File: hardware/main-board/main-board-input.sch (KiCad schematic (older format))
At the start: 11 parts

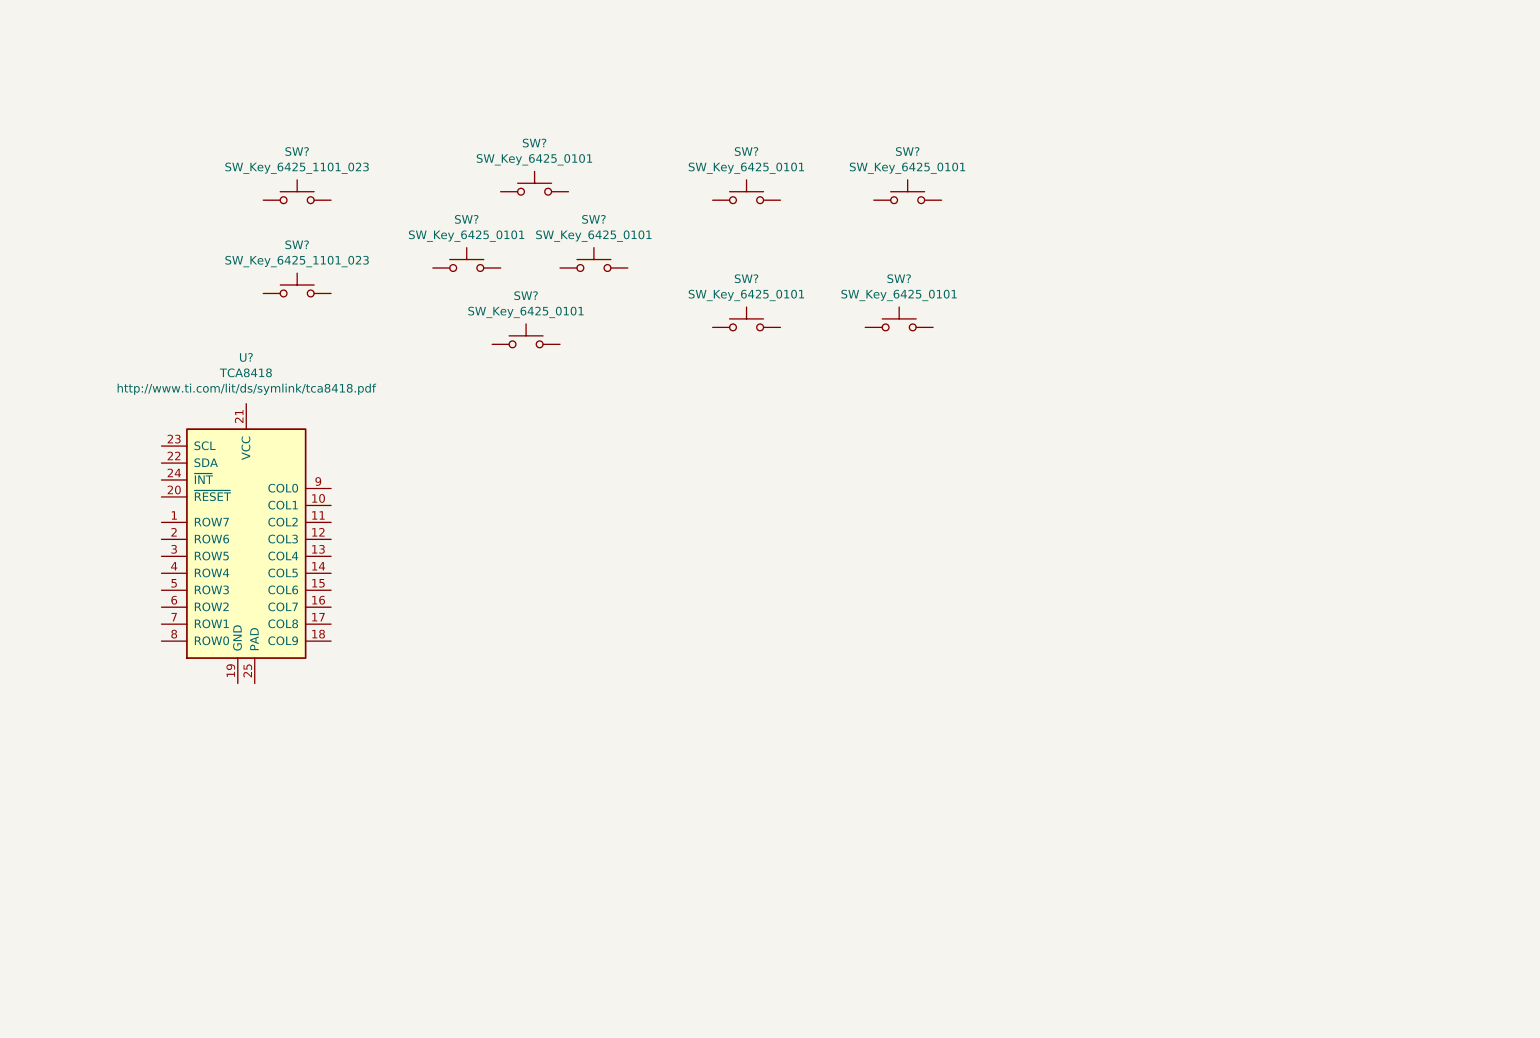
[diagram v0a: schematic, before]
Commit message: Starting to put main board MCU components in place
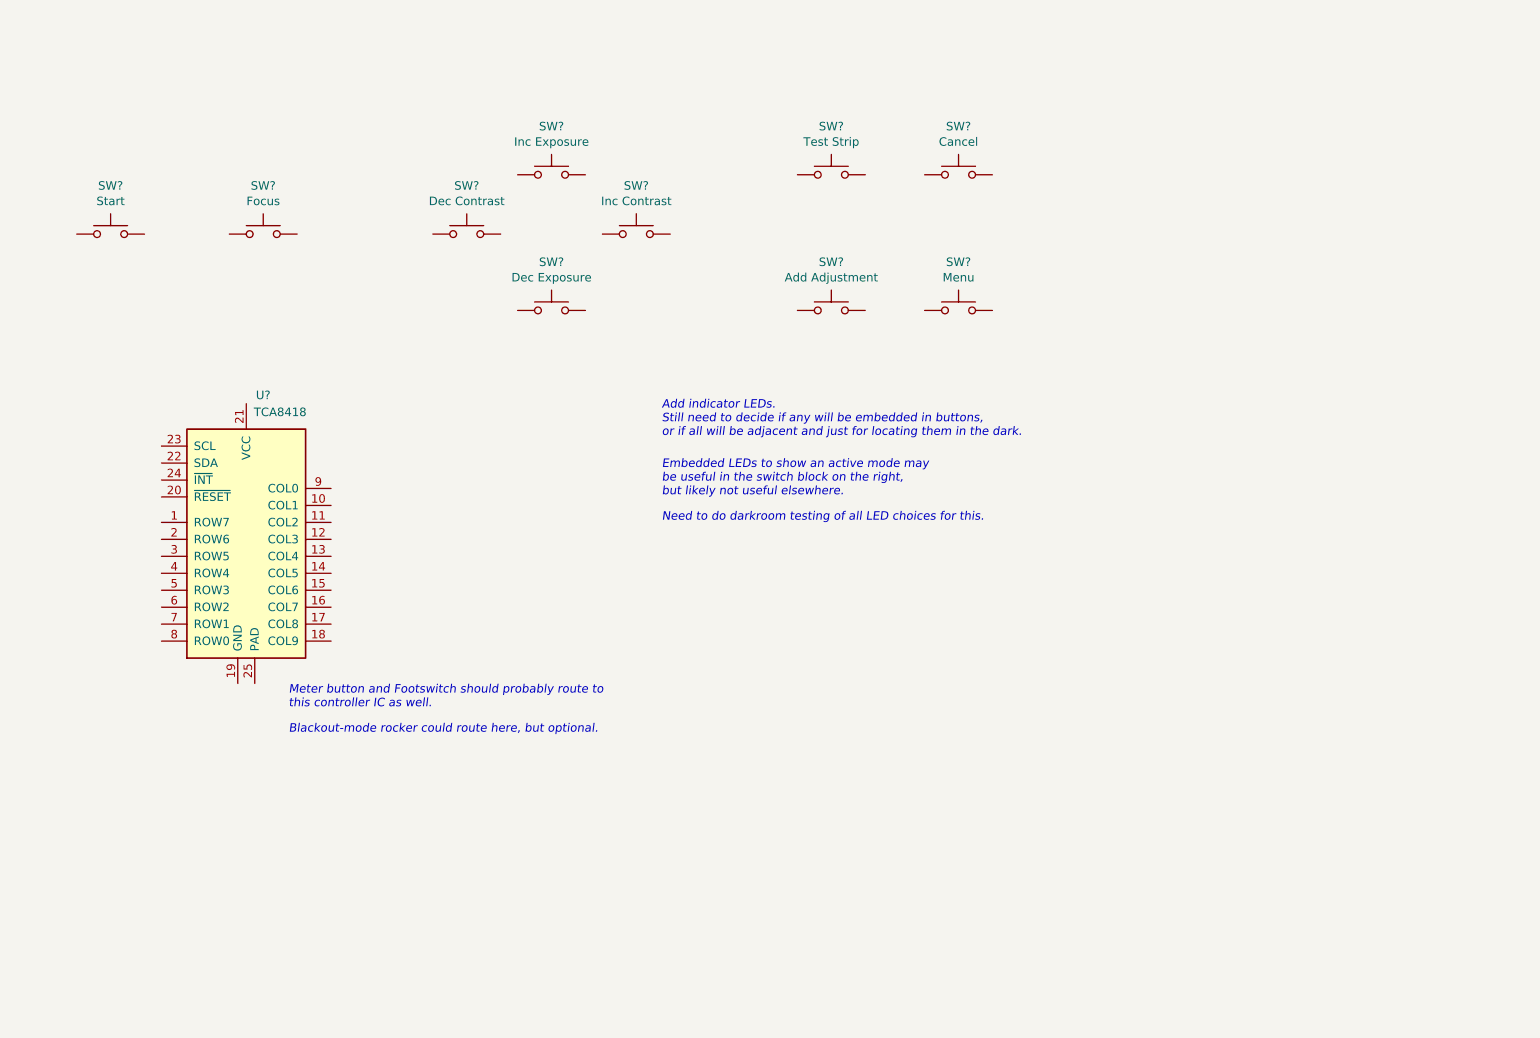
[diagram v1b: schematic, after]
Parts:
- SW?: value SW_Key_6425_1101_023 -> Start; footprint (none) -> lib_fp:SW_Key_6425_1101_023
- SW?: value SW_Key_6425_1101_023 -> Focus; footprint (none) -> lib_fp:SW_Key_6425_1101_023
- SW?: value SW_Key_6425_0101 -> Inc Exposure
- SW?: value SW_Key_6425_0101 -> Dec Contrast
- SW?: value SW_Key_6425_0101 -> Inc Contrast
- SW?: value SW_Key_6425_0101 -> Dec Exposure
- SW?: value SW_Key_6425_0101 -> Test Strip
- SW?: value SW_Key_6425_0101 -> Add Adjustment
- SW?: value SW_Key_6425_0101 -> Cancel
- SW?: value SW_Key_6425_0101 -> Menu
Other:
- note added: "Add indicator LEDs.\nStill need to decide if any will be embedded in buttons,\nor if all will be adjacent and just for locating them in the dark."
- note added: "Blackout-mode rocker could route here, but optional."
- note added: "Embedded LEDs to show an active mode may\nbe useful in the switch block on the right,\nbut likely not useful elsewhere."
- note added: "Meter button and Footswitch should probably route to\nthis controller IC as well."
- note added: "Need to do darkroom testing of all LED choices for this."
- moved on the sheet: SW?
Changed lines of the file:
@@
 $Descr USLetter 11000 8500
 encoding utf-8
-Sheet 3 3
+Sheet 3 4
 Title "Printalyzer - Main Board"
 Date ""
@@
 L Marquadt_Switch:SW_Key_6425_1101_023 SW?
 U 1 1 5F8B879A
-P 2300 1800
-F 0 "SW?" H 2300 2085 50  0000 C CNN
-F 1 "SW_Key_6425_1101_023" H 2300 1994 50  0000 C CNN
-F 2 "" H 2300 2000 50  0001 C CNN
-F 3 "https://www.marquardt-switches.com/PLM-uploads/kzeichnung/64251101_00_K.pdf" H 2300 2000 50  0001 C CNN
-	1    2300 1800
+P 1200 2000
+F 0 "SW?" H 1200 2285 50  0000 C CNN
+F 1 "Start" H 1200 2194 50  0000 C CNN
+F 2 "lib_fp:SW_Key_6425_1101_023" H 1200 2200 50  0001 C CNN
+F 3 "https://www.marquardt-switches.com/PLM-uploads/kzeichnung/64251101_00_K.pdf" H 1200 2200 50  0001 C CNN
+	1    1200 2000
 	1    0    0    -1
 $EndComp
@@
 L Marquadt_Switch:SW_Key_6425_1101_023 SW?
 U 1 1 5F8B9734
-P 2300 2350
-F 0 "SW?" H 2300 2635 50  0000 C CNN
-F 1 "SW_Key_6425_1101_023" H 2300 2544 50  0000 C CNN
-F 2 "" H 2300 2550 50  0001 C CNN
-F 3 "https://www.marquardt-switches.com/PLM-uploads/kzeichnung/64251101_00_K.pdf" H 2300 2550 50  0001 C CNN
-	1    2300 2350
+P 2100 2000
+F 0 "SW?" H 2100 2285 50  0000 C CNN
+F 1 "Focus" H 2100 2194 50  0000 C CNN
+F 2 "lib_fp:SW_Key_6425_1101_023" H 2100 2200 50  0001 C CNN
+F 3 "https://www.marquardt-switches.com/PLM-uploads/kzeichnung/64251101_00_K.pdf" H 2100 2200 50  0001 C CNN
+	1    2100 2000
 	1    0    0    -1
 $EndComp
@@
 L Marquadt_Switch:SW_Key_6425_0101 SW?
 U 1 1 5F8B9EB7
-P 3700 1750
-F 0 "SW?" H 3700 2035 50  0000 C CNN
-F 1 "SW_Key_6425_0101" H 3700 1944 50  0000 C CNN
-F 2 "lib_fp:SW_Key_6425_0101" H 3700 1950 50  0001 C CNN
-F 3 "https://www.marquardt-switches.com/PLM-uploads/kzeichnung/64250101_00_K.pdf" H 3700 1950 50  0001 C CNN
-	1    3700 1750
+P 3800 1650
+F 0 "SW?" H 3800 1935 50  0000 C CNN
+F 1 "Inc Exposure" H 3800 1844 50  0000 C CNN
+F 2 "lib_fp:SW_Key_6425_0101" H 3800 1850 50  0001 C CNN
+F 3 "https://www.marquardt-switches.com/PLM-uploads/kzeichnung/64250101_00_K.pdf" H 3800 1850 50  0001 C CNN
+	1    3800 1650
 	1    0    0    -1
 $EndComp
@@
 L Marquadt_Switch:SW_Key_6425_0101 SW?
 U 1 1 5F8BA3E3
-P 3300 2200
-F 0 "SW?" H 3300 2485 50  0000 C CNN
-F 1 "SW_Key_6425_0101" H 3300 2394 50  0000 C CNN
-F 2 "lib_fp:SW_Key_6425_0101" H 3300 2400 50  0001 C CNN
-F 3 "https://www.marquardt-switches.com/PLM-uploads/kzeichnung/64250101_00_K.pdf" H 3300 2400 50  0001 C CNN
-	1    3300 2200
+P 3300 2000
+F 0 "SW?" H 3300 2285 50  0000 C CNN
+F 1 "Dec Contrast" H 3300 2194 50  0000 C CNN
+F 2 "lib_fp:SW_Key_6425_0101" H 3300 2200 50  0001 C CNN
+F 3 "https://www.marquardt-switches.com/PLM-uploads/kzeichnung/64250101_00_K.pdf" H 3300 2200 50  0001 C CNN
+	1    3300 2000
 	1    0    0    -1
 $EndComp
@@
 L Marquadt_Switch:SW_Key_6425_0101 SW?
 U 1 1 5F8BA80F
-P 4050 2200
-F 0 "SW?" H 4050 2485 50  0000 C CNN
-F 1 "SW_Key_6425_0101" H 4050 2394 50  0000 C CNN
-F 2 "lib_fp:SW_Key_6425_0101" H 4050 2400 50  0001 C CNN
-F 3 "https://www.marquardt-switches.com/PLM-uploads/kzeichnung/64250101_00_K.pdf" H 4050 2400 50  0001 C CNN
-	1    4050 2200
+P 4300 2000
+F 0 "SW?" H 4300 2285 50  0000 C CNN
+F 1 "Inc Contrast" H 4300 2194 50  0000 C CNN
+F 2 "lib_fp:SW_Key_6425_0101" H 4300 2200 50  0001 C CNN
+F 3 "https://www.marquardt-switches.com/PLM-uploads/kzeichnung/64250101_00_K.pdf" H 4300 2200 50  0001 C CNN
+	1    4300 2000
 	1    0    0    -1
 $EndComp
@@
 L Marquadt_Switch:SW_Key_6425_0101 SW?
 U 1 1 5F8BAD5B
-P 3650 2650
-F 0 "SW?" H 3650 2935 50  0000 C CNN
-F 1 "SW_Key_6425_0101" H 3650 2844 50  0000 C CNN
-F 2 "lib_fp:SW_Key_6425_0101" H 3650 2850 50  0001 C CNN
-F 3 "https://www.marquardt-switches.com/PLM-uploads/kzeichnung/64250101_00_K.pdf" H 3650 2850 50  0001 C CNN
-	1    3650 2650
+P 3800 2450
+F 0 "SW?" H 3800 2735 50  0000 C CNN
+F 1 "Dec Exposure" H 3800 2644 50  0000 C CNN
+F 2 "lib_fp:SW_Key_6425_0101" H 3800 2650 50  0001 C CNN
+F 3 "https://www.marquardt-switches.com/PLM-uploads/kzeichnung/64250101_00_K.pdf" H 3800 2650 50  0001 C CNN
+	1    3800 2450
 	1    0    0    -1
 $EndComp
@@
 L Marquadt_Switch:SW_Key_6425_0101 SW?
 U 1 1 5F8BB404
-P 4950 1800
-F 0 "SW?" H 4950 2085 50  0000 C CNN
-F 1 "SW_Key_6425_0101" H 4950 1994 50  0000 C CNN
-F 2 "lib_fp:SW_Key_6425_0101" H 4950 2000 50  0001 C CNN
-F 3 "https://www.marquardt-switches.com/PLM-uploads/kzeichnung/64250101_00_K.pdf" H 4950 2000 50  0001 C CNN
-	1    4950 1800
+P 5450 1650
+F 0 "SW?" H 5450 1935 50  0000 C CNN
+F 1 "Test Strip" H 5450 1844 50  0000 C CNN
+F 2 "lib_fp:SW_Key_6425_0101" H 5450 1850 50  0001 C CNN
+F 3 "https://www.marquardt-switches.com/PLM-uploads/kzeichnung/64250101_00_K.pdf" H 5450 1850 50  0001 C CNN
+	1    5450 1650
 	1    0    0    -1
 $EndComp
@@
 L Marquadt_Switch:SW_Key_6425_0101 SW?
 U 1 1 5F8BB964
-P 4950 2550
-F 0 "SW?" H 4950 2835 50  0000 C CNN
-F 1 "SW_Key_6425_0101" H 4950 2744 50  0000 C CNN
-F 2 "lib_fp:SW_Key_6425_0101" H 4950 2750 50  0001 C CNN
-F 3 "https://www.marquardt-switches.com/PLM-uploads/kzeichnung/64250101_00_K.pdf" H 4950 2750 50  0001 C CNN
-	1    4950 2550
+P 5450 2450
+F 0 "SW?" H 5450 2735 50  0000 C CNN
+F 1 "Add Adjustment" H 5450 2644 50  0000 C CNN
+F 2 "lib_fp:SW_Key_6425_0101" H 5450 2650 50  0001 C CNN
+F 3 "https://www.marquardt-switches.com/PLM-uploads/kzeichnung/64250101_00_K.pdf" H 5450 2650 50  0001 C CNN
+	1    5450 2450
 	1    0    0    -1
 $EndComp
@@
 L Marquadt_Switch:SW_Key_6425_0101 SW?
 U 1 1 5F8BBE5F
-P 5900 1800
-F 0 "SW?" H 5900 2085 50  0000 C CNN
-F 1 "SW_Key_6425_0101" H 5900 1994 50  0000 C CNN
-F 2 "lib_fp:SW_Key_6425_0101" H 5900 2000 50  0001 C CNN
-F 3 "https://www.marquardt-switches.com/PLM-uploads/kzeichnung/64250101_00_K.pdf" H 5900 2000 50  0001 C CNN
-	1    5900 1800
+P 6200 1650
+F 0 "SW?" H 6200 1935 50  0000 C CNN
+F 1 "Cancel" H 6200 1844 50  0000 C CNN
+F 2 "lib_fp:SW_Key_6425_0101" H 6200 1850 50  0001 C CNN
+F 3 "https://www.marquardt-switches.com/PLM-uploads/kzeichnung/64250101_00_K.pdf" H 6200 1850 50  0001 C CNN
+	1    6200 1650
 	1    0    0    -1
 $EndComp
@@
 L Marquadt_Switch:SW_Key_6425_0101 SW?
 U 1 1 5F8BC2B0
-P 5850 2550
-F 0 "SW?" H 5850 2835 50  0000 C CNN
-F 1 "SW_Key_6425_0101" H 5850 2744 50  0000 C CNN
-F 2 "lib_fp:SW_Key_6425_0101" H 5850 2750 50  0001 C CNN
-F 3 "https://www.marquardt-switches.com/PLM-uploads/kzeichnung/64250101_00_K.pdf" H 5850 2750 50  0001 C CNN
-	1    5850 2550
+P 6200 2450
+F 0 "SW?" H 6200 2735 50  0000 C CNN
+F 1 "Menu" H 6200 2644 50  0000 C CNN
+F 2 "lib_fp:SW_Key_6425_0101" H 6200 2650 50  0001 C CNN
+F 3 "https://www.marquardt-switches.com/PLM-uploads/kzeichnung/64250101_00_K.pdf" H 6200 2650 50  0001 C CNN
+	1    6200 2450
 	1    0    0    -1
 $EndComp
@@
 U 1 1 5F8B6B00
 P 2000 3850
-F 0 "U?" H 2000 4971 50  0000 C CNN
-F 1 "TCA8418" H 2000 4880 50  0000 C CNN
+F 0 "U?" H 2100 4750 50  0000 C CNN
+F 1 "TCA8418" H 2200 4650 50  0000 C CNN
 F 2 "lib_fp:WQFN-24-1EP_4x4mm_P0.5mm_EP2.45x2.45mm" H 2600 3750 50  0001 C CNN
-F 3 "http://www.ti.com/lit/ds/symlink/tca8418.pdf" H 2000 4789 50  0000 C CNN
+F 3 "http://www.ti.com/lit/ds/symlink/tca8418.pdf" H 2000 4789 50  0001 C CNN
 	1    2000 3850
 	1    0    0    -1
 $EndComp
+Text Notes 4450 3200 0    50   Italic 0
+Add indicator LEDs.\nStill need to decide if any will be embedded in buttons,\nor if all will be adjacent and just for locating them in the dark.
+Text Notes 4450 3550 0    50   Italic 0
+Embedded LEDs to show an active mode may\nbe useful in the switch block on the right,\nbut likely not useful elsewhere.
+Text Notes 4450 3700 0    50   Italic 0
+Need to do darkroom testing of all LED choices for this.
+Text Notes 2250 4800 0    50   Italic 0
+Meter button and Footswitch should probably route to\nthis controller IC as well.
+Text Notes 2250 4950 0    50   Italic 0
+Blackout-mode rocker could route here, but optional.
 $EndSCHEMATC

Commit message: More work on main board input and panel connection sheets
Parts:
- added C?: 0.1uF, symbol Device:C_Small
- added D1, D10, D2, D3, D4, D5, D6, D7, D8, D9: LED, symbol Device:LED_ALT
- added J?: Blackout Switch, Connector_PinHeader_2.54mm:PinHeader_1x02_P2.54mm_Vertical, symbol Connector_Generic:Conn_01x02
- added R? (x3): 10K, symbol Device:R_Small
- SW10, SW7, SW8, SW9: renamed from SW?; footprint lib_fp:SW_Key_6425_0101 -> lib_fp:SW_Key_6425_0101_LED; symbol Marquadt_Switch:SW_Key_6425_0101 -> Marquadt_Switch:SW_Key_6425_0101_LED
- gave numbers to parts that had none: 6
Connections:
- net at U?.1 (ROW7): now also U?.2 (ROW6), U?.3 (ROW5), U?.4 (ROW4), U?.5 (ROW3), R?.2
- net BTN2: now reaches U?.10 (COL1)
- net BTN2: now also SW2.1
- net BTN3: now reaches U?.11 (COL2)
- net BTN3: now also SW3.1
- net BTN4: now reaches U?.12 (COL3)
- net BTN4: now also SW4.1
- net BTN5: now reaches U?.13 (COL4)
- net BTN5: now also SW5.1
- net BTN6: now reaches U?.14 (COL5)
- net BTN6: now also SW6.1
- net BTN7: now reaches U?.15 (COL6)
- net BTN7: now also SW7.1
- net BTN8: now reaches U?.16 (COL7)
- net BTN8: now also SW8.1
- net BTN9: now reaches U?.17 (COL8)
- net BTN9: now also SW9.1
- net BTN10: now reaches U?.18 (COL9)
- net BTN10: now also SW10.1
- net GND: now reaches U?.19 (GND)
- net GND: now also SW1.2, SW10.2, SW2.2, SW3.2, SW4.2, SW5.2, SW6.2, SW7.2, SW8.2, SW9.2, U?.25 (PAD), C?.1, J?.2 (Pin_2)
- net at U?.20 (~RESET~): now also R?.2
- net +3V3: now reaches U?.21 (VCC)
- net +3V3: now also SW10.4 (A), SW7.4 (A), SW8.4 (A), SW9.4 (A), C?.2, D1.2 (A), D10.2 (A), D2.2 (A), D3.2 (A), D4.2 (A), D5.2 (A), D6.2 (A), D7.2 (A), D8.2 (A), D9.2 (A), R?.1, R?.1, R?.1
- net INT_I2C_SDA: now reaches U?.22 (SDA)
- net INT_I2C_SCL: now reaches U?.23 (SCL)
- net KEY_INT: now reaches U?.24 (~INT~)
- net KEY_INT: now also R?.2
- net SENSOR_BTN: now reaches U?.6 (ROW2)
- net FOOTSWITCH: now reaches U?.7 (ROW1)
- net BLACKOUT_SW: now reaches U?.8 (ROW0)
- net BLACKOUT_SW: now also J?.1 (Pin_1)
- net BTN1: now reaches U?.9 (COL0)
- net BTN1: now also SW1.1
- new net IND1: D1.1 (K)
- new net IND10: D10.1 (K)
- new net IND10_T: SW10.3 (K)
- new net IND2: D2.1 (K)
- new net IND3: D3.1 (K)
- new net IND4: D4.1 (K)
- new net IND5: D5.1 (K)
- new net IND6: D6.1 (K)
- new net IND7: D7.1 (K)
- new net IND7_T: SW7.3 (K)
- new net IND8: D8.1 (K)
- new net IND8_T: SW8.3 (K)
- new net IND9: D9.1 (K)
- new net IND9_T: SW9.3 (K)
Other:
- note added: "Considering cheap/fancy driver IC for all the LEDs,\nadd after bench testing."
- note removed: "Add indicator LEDs.\nStill need to decide if any will be embedded in buttons,\nor if all will be adjacent and just for locating them in the dark."
- note removed: "Blackout-mode rocker could route here, but optional."
- note removed: "Embedded LEDs to show an active mode may\nbe useful in the switch block on the right,\nbut likely not useful elsewhere."
- note removed: "Meter button and Footswitch should probably route to\nthis controller IC as well."
- moved on the sheet: SW1, SW2, SW3, SW4, SW5, SW6, U?
